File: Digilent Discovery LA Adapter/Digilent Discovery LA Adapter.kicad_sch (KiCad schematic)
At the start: 5 parts, among them J1 Cerberus_Expansion, J2 Card_Header, J4 XE_Header

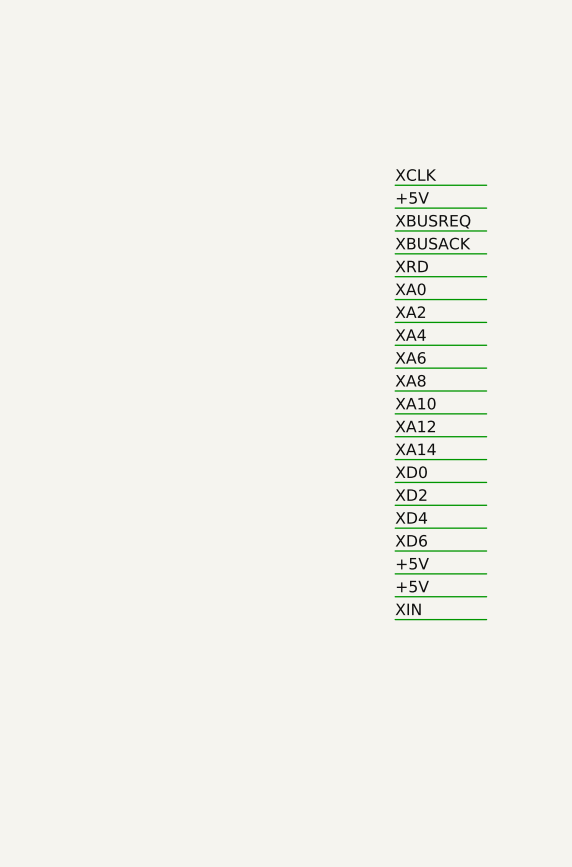
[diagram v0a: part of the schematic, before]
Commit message: Copied Sch headers from Mega IIe
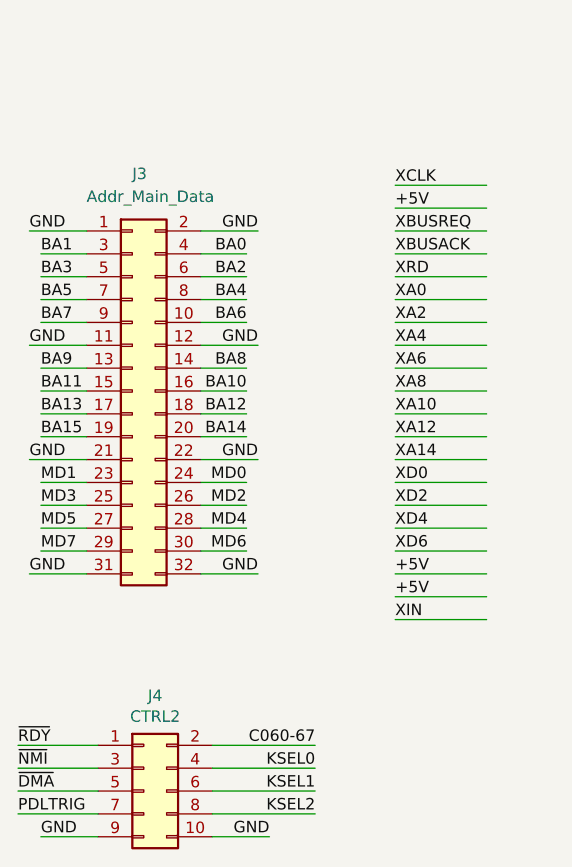
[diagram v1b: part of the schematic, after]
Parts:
- added J3: Addr_Main_Data, Connector_PinSocket_2.54mm:PinSocket_2x16_P2.54mm_Vertical, symbol Connector_Generic:Conn_02x16_Odd_Even
- added J4: CTRL2, Connector_PinSocket_2.54mm:PinSocket_2x05_P2.54mm_Vertical, symbol Connector_Generic:Conn_02x05_Odd_Even
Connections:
- net GND: now also J3.1 (Pin_1), J3.11 (Pin_11), J3.12 (Pin_12), J3.2 (Pin_2), J3.21 (Pin_21), J3.22 (Pin_22), J3.31 (Pin_31), J3.32 (Pin_32), J4.10 (Pin_10), J4.9 (Pin_9)
- new net BA0: J3.4 (Pin_4)
- new net BA1: J3.3 (Pin_3)
- new net BA10: J3.16 (Pin_16)
- new net BA11: J3.15 (Pin_15)
- new net BA12: J3.18 (Pin_18)
- new net BA13: J3.17 (Pin_17)
- new net BA14: J3.20 (Pin_20)
- new net BA15: J3.19 (Pin_19)
- new net BA2: J3.6 (Pin_6)
- new net BA3: J3.5 (Pin_5)
- new net BA4: J3.8 (Pin_8)
- new net BA5: J3.7 (Pin_7)
- new net BA6: J3.10 (Pin_10)
- new net BA7: J3.9 (Pin_9)
- new net BA8: J3.14 (Pin_14)
- new net BA9: J3.13 (Pin_13)
- new net C060-67: J4.2 (Pin_2)
- new net KSEL0: J4.4 (Pin_4)
- new net KSEL1: J4.6 (Pin_6)
- new net KSEL2: J4.8 (Pin_8)
- new net MD0: J3.24 (Pin_24)
- new net MD1: J3.23 (Pin_23)
- new net MD2: J3.26 (Pin_26)
- new net MD3: J3.25 (Pin_25)
- new net MD4: J3.28 (Pin_28)
- new net MD5: J3.27 (Pin_27)
- new net MD6: J3.30 (Pin_30)
- new net MD7: J3.29 (Pin_29)
- new net PDLTRIG: J4.7 (Pin_7)
- new net ~{DMA}: J4.5 (Pin_5)
- new net ~{NMI}: J4.3 (Pin_3)
- new net ~{RDY}: J4.1 (Pin_1)
